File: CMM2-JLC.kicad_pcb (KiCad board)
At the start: 2 copper layers, 49 parts, among them J1 Nunchuck, U1 STM32H743IITx, U2 MT48LC16M16A2P

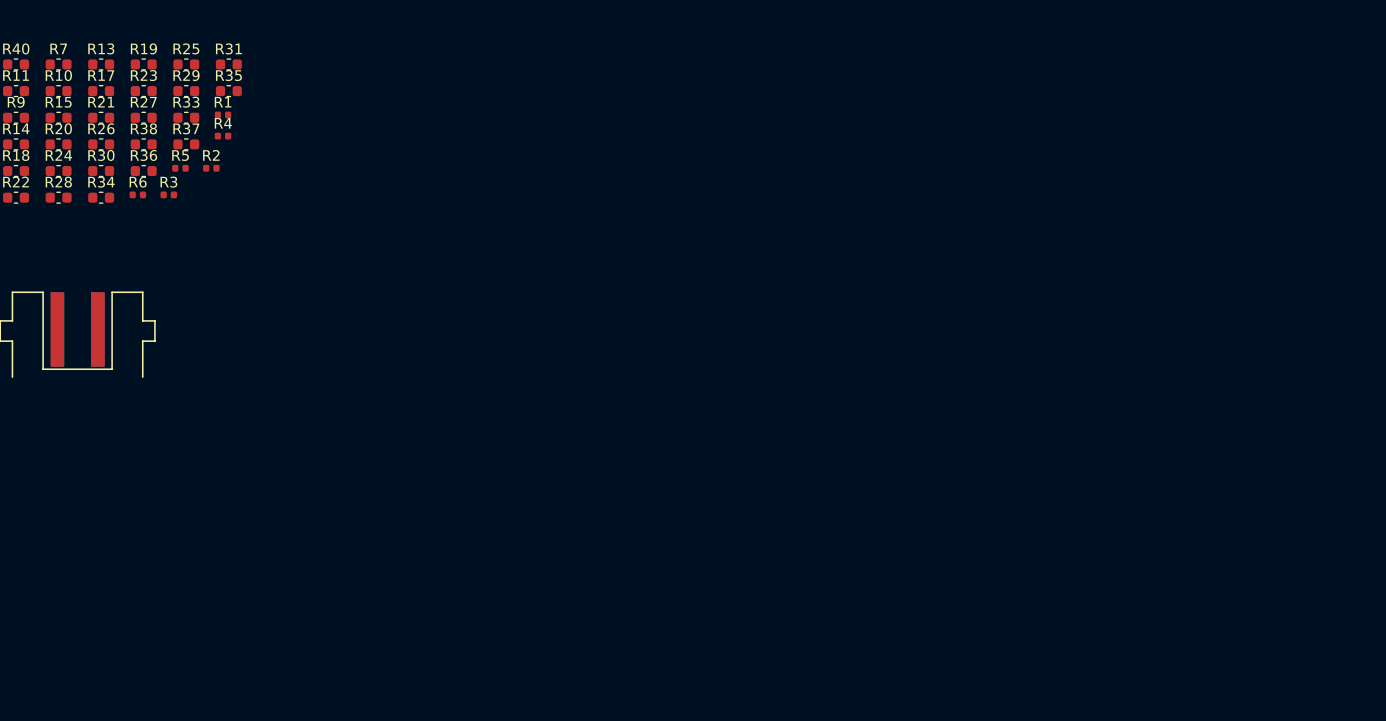
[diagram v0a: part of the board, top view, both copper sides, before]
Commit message: Add footprints and crystals
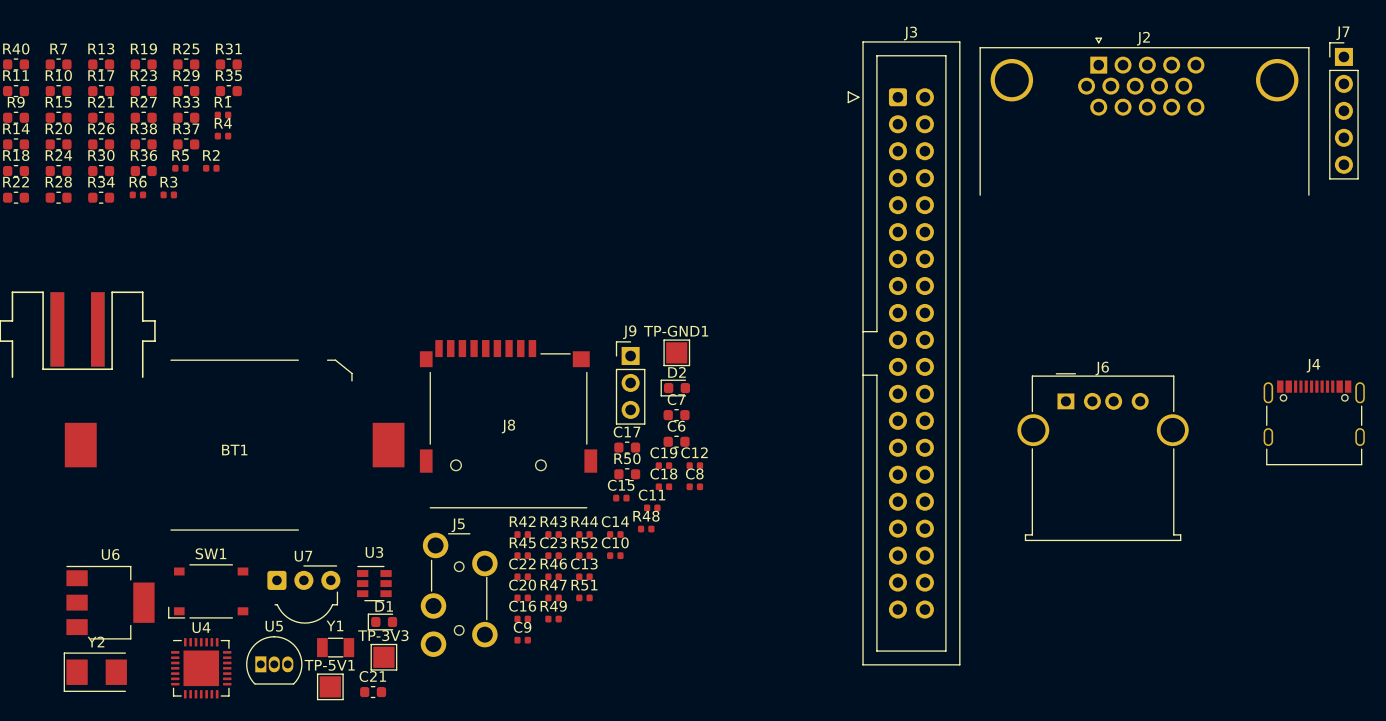
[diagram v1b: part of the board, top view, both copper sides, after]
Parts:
- added BT1: CR2032, CMM2-JLC:BatteryHolder_CR2032-BS-6-1, F.Cu at (110.4, 65.5)
- added C10: 6p, Capacitor_SMD:C_0402_1005Metric, F.Cu at (146.3, 75.9)
- added C11: 20p, Capacitor_SMD:C_0402_1005Metric, F.Cu at (149.7, 71.4)
- added C12: 20p, Capacitor_SMD:C_0402_1005Metric, F.Cu at (153.8, 67.4)
- added C13: 1u, Capacitor_SMD:C_0402_1005Metric, F.Cu at (143.3, 77.9)
- added C14: 100n, Capacitor_SMD:C_0402_1005Metric, F.Cu at (146.3, 73.9)
- added C15: 4.7u, Capacitor_SMD:C_0402_1005Metric, F.Cu at (146.8, 70.5)
- added C16: 100n, Capacitor_SMD:C_0402_1005Metric, F.Cu at (137.5, 81.9)
- added C17: 10u, Capacitor_SMD:C_0603_1608Metric, F.Cu at (147.4, 65.7)
- added C18: 100n, Capacitor_SMD:C_0402_1005Metric, F.Cu at (150.8, 69.4)
- added C19: 1u, Capacitor_SMD:C_0402_1005Metric, F.Cu at (150.8, 67.4)
- added C20: 100n, Capacitor_SMD:C_0402_1005Metric, F.Cu at (137.5, 79.9)
- added C21: 22u, Capacitor_SMD:C_0603_1608Metric, F.Cu at (123.4, 88.8)
- added C22: 100n, Capacitor_SMD:C_0402_1005Metric, F.Cu at (137.5, 77.9)
- added C23: 100n, Capacitor_SMD:C_0402_1005Metric, F.Cu at (140.4, 75.9)
- added C6: 2.2u, Capacitor_SMD:C_0603_1608Metric, F.Cu at (152.0, 65.2)
- added C7: 2.2u, Capacitor_SMD:C_0603_1608Metric, F.Cu at (152.0, 62.7)
- added C8: 1u, Capacitor_SMD:C_0402_1005Metric, F.Cu at (153.8, 69.4)
- added C9: 6p, Capacitor_SMD:C_0402_1005Metric, F.Cu at (137.5, 83.9)
- added D1: SD CARD / RED, LED_SMD:LED_0603_1608Metric, F.Cu at (124.5, 82.2)
- added D2: POWER / GREEN, LED_SMD:LED_0603_1608Metric, F.Cu at (152.1, 60.1)
- added J2: VGA, Connector_Dsub:DSUB-15-HD_Male_Horizontal_P2.29x1.98mm_EdgePinOffset8.35mm_Housed_MountingHolesOffset10.89mm, F.Cu at (191.8, 29.7)
- added J3: EXTERNAL I/O, Connector_IDC:IDC-Header_2x20_P2.54mm_Vertical, F.Cu at (172.9, 32.7)
- added J4: USB_C_Receptacle_USB2.0, Connector_USB:USB_C_Receptacle_Palconn_UTC16-G, F.Cu at (212.1, 62.5)
- added J5: Audio, CMM2-JLC:PJ-3270, F.Cu at (131.6, 86.0)
- added J6: USB A Host, Connector_USB:USB_A_Molex_67643_Horizontal, F.Cu at (188.7, 61.4)
- added J7: SWD, Connector_PinHeader_2.54mm:PinHeader_1x05_P2.54mm_Vertical, F.Cu at (214.9, 28.9)
- added J8: Micro_SD_Card_Det, CMM2-JLC:HOAUC_HYC77-TF09-200, F.Cu at (131.2, 67.4)
- added J9: Boot select, Connector_PinHeader_2.54mm:PinHeader_1x03_P2.54mm_Vertical, F.Cu at (147.7, 57.1)
- added R42: 10k, Resistor_SMD:R_0402_1005Metric, F.Cu at (137.5, 73.9)
- added R43: 10R, Resistor_SMD:R_0402_1005Metric, F.Cu at (140.4, 73.9)
- added R44: 5.1k, Resistor_SMD:R_0402_1005Metric, F.Cu at (143.3, 73.9)
- added R45: 5.1k, Resistor_SMD:R_0402_1005Metric, F.Cu at (137.5, 75.9)
- added R46: 4.7k, Resistor_SMD:R_0402_1005Metric, F.Cu at (140.4, 77.9)
- added R47: 3.3k, Resistor_SMD:R_0402_1005Metric, F.Cu at (140.4, 79.9)
- added R48: 4.7k, Resistor_SMD:R_0402_1005Metric, F.Cu at (149.2, 73.4)
- added R49: 4.7k, Resistor_SMD:R_0402_1005Metric, F.Cu at (140.4, 81.9)
- added R50: 120R, Resistor_SMD:R_0603_1608Metric, F.Cu at (147.4, 68.2)
- added R51: 100k, Resistor_SMD:R_0402_1005Metric, F.Cu at (143.3, 79.9)
- added R52: 10k, Resistor_SMD:R_0402_1005Metric, F.Cu at (143.3, 75.9)
- added SW1: Reset, CMM2-JLC:TS-1187A-X-X-X, F.Cu at (108.2, 79.3)
- added TP-3V3: TestPoint, TestPoint:TestPoint_Pad_2.0x2.0mm, F.Cu at (124.5, 85.5)
- added TP-5V1: TestPoint, TestPoint:TestPoint_Pad_2.0x2.0mm, F.Cu at (119.4, 88.3)
- added TP-GND1: TestPoint, TestPoint:TestPoint_Pad_2.0x2.0mm, F.Cu at (152.1, 56.8)
- added U3: SRV05-4, Package_TO_SOT_SMD:SOT-23-6, F.Cu at (123.6, 78.5)
- added U4: CP2102N-A01-GQFN28, Package_DFN_QFN:QFN-28-1EP_5x5mm_P0.5mm_EP3.35x3.35mm, F.Cu at (107.2, 86.5)
- added U5: DS18B20, Package_TO_SOT_THT:TO-92_Inline, F.Cu at (112.9, 86.2)
- added U6: AMS1117-3.3, Package_TO_SOT_SMD:SOT-223-3_TabPin2, F.Cu at (98.7, 80.3)
- added U7: TSOP4838, OptoDevice:Vishay_MOLD-3Pin, F.Cu at (114.4, 78.2)
- added Y1: 32.768 kHz, Crystal:Crystal_SMD_3215-2Pin_3.2x1.5mm, F.Cu at (119.9, 84.6)
- added Y2: 8 MHz, Crystal:Crystal_SMD_5032-2Pin_5.0x3.2mm, F.Cu at (97.4, 86.9)
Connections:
- net Net-(U1-Pad119) renamed /PA8
- U1 pad 120: Net-(U1-Pad120) -> /PA9
- U1 pad 121: Net-(U1-Pad121) -> /PA10
- U1 pad 122: Net-(U1-Pad122) -> /PA11
- U1 pad 123: Net-(U1-Pad123) -> /PA12
- U1 pad 124: Net-(U1-Pad124) -> /PA13
- U1 pad 137: Net-(U1-Pad137) -> /PA14
- U1 pad 138: Net-(U1-Pad138) -> /PA15
- U1 pad 166: Net-(U1-Pad166) -> /BOOT0
- U1 pad 31: Net-(U1-Pad31) -> /RESET
- U1 pad 40: Net-(U1-Pad40) -> /PA0
- U1 pad 41: Net-(U1-Pad41) -> /PA1
- U1 pad 42: Net-(U1-Pad42) -> /PA2
- U1 pad 47: Net-(U1-Pad47) -> /PA3
- U1 pad 50: Net-(U1-Pad50) -> /PA4
- U1 pad 51: Net-(U1-Pad51) -> /PA5
- U1 pad 52: Net-(U1-Pad52) -> /PA6
- U1 pad 53: Net-(U1-Pad53) -> /PA7
- U1 pad 6: Net-(U1-Pad6) -> /VBAT
- U1 pad 89: /PH12 -> GND

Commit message: Add board outline
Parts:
- moved J7 297.8 mm to (512.7, 30.5)
- moved R48 297.8 mm to (447.0, 75.0)
- moved C1 297.8 mm to (329.8, 59.2)
- moved C10 297.8 mm to (444.1, 77.5)
- moved C11 297.8 mm to (447.5, 73.0)
- moved C12 297.8 mm to (451.6, 69.0)
- moved C14 297.8 mm to (444.1, 75.5)
- moved C17 297.8 mm to (445.2, 67.3)
- moved C21 297.8 mm to (421.2, 90.4)
- moved C23 297.8 mm to (438.2, 77.5)
- moved C4 297.8 mm to (329.8, 61.2)
- moved C8 297.8 mm to (451.6, 71.0)
- moved D2 297.8 mm to (449.9, 61.7)
- moved J2 297.8 mm to (489.6, 31.3)
- moved J3 297.8 mm to (470.7, 34.3)
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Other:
- board outline added: 130 x 102 mm
- copper layers 2 -> 4
- net class Default: clearance 0.2 -> 0.127; trace_width 0.25 -> 0.127; via_dia 0.8 -> 0.45; via_drill 0.4 -> 0.2
- rule pad_to_mask_clearance: 0.05 -> 0.01
- rule trace_clearance: 0.2 -> 0.127
- rule trace_min: 0.2 -> 0.127
- rule via_min_drill: 0.3 -> 0.2
- rule via_min_size: 0.4 -> 0.45

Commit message: first sdram routing
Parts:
- removed BT1: CR2032, CMM2-JLC:BatteryHolder_CR2032-BS-6-1
- removed C1, C14, C16, C18, C2, C20, C22, C23, C3, C4, C5: 100n, Capacitor_SMD:C_0402_1005Metric
- removed C10, C9: 6p, Capacitor_SMD:C_0402_1005Metric
- removed C11, C12: 20p, Capacitor_SMD:C_0402_1005Metric
- removed C13, C19, C8: 1u, Capacitor_SMD:C_0402_1005Metric
- removed C15: 4.7u, Capacitor_SMD:C_0402_1005Metric
- removed C17: 10u, Capacitor_SMD:C_0603_1608Metric
- removed C21: 22u, Capacitor_SMD:C_0603_1608Metric
- removed C6, C7: 2.2u, Capacitor_SMD:C_0603_1608Metric
- removed D1: SD CARD / RED, LED_SMD:LED_0603_1608Metric
- removed D2: POWER / GREEN, LED_SMD:LED_0603_1608Metric
- removed J2: VGA, Connector_Dsub:DSUB-15-HD_Male_Horizontal_P2.29x1.98mm_EdgePinOffset8.35mm_Housed_MountingHolesOffset10.89mm
- removed J3: EXTERNAL I/O, Connector_IDC:IDC-Header_2x20_P2.54mm_Vertical
- removed J4: USB_C_Receptacle_USB2.0, Connector_USB:USB_C_Receptacle_Palconn_UTC16-G
- removed J5: Audio, CMM2-JLC:PJ-3270
- removed J6: USB A Host, Connector_USB:USB_A_Molex_67643_Horizontal
- removed J7: SWD, Connector_PinHeader_2.54mm:PinHeader_1x05_P2.54mm_Vertical
- removed J8: Micro_SD_Card_Det, CMM2-JLC:HOAUC_HYC77-TF09-200
- removed J9: Boot select, Connector_PinHeader_2.54mm:PinHeader_1x03_P2.54mm_Vertical
- removed R1, R2, R3, R4, R42, R5, R52, R6: 10k, Resistor_SMD:R_0402_1005Metric
- removed R10, R11, R12, R16, R17, R18, R22, R23, R24, R28, R29, R30, R34, R36, R37, R40, R7, R8, R9: 240R, Resistor_SMD:R_0603_1608Metric
- removed R13, R14, R15, R19, R20, R21, R25, R26, R27, R31, R32, R33, R39, R50: 120R, Resistor_SMD:R_0603_1608Metric
- removed R35, R38, R41: 75R, Resistor_SMD:R_0603_1608Metric
- removed R43: 10R, Resistor_SMD:R_0402_1005Metric
- removed R44, R45: 5.1k, Resistor_SMD:R_0402_1005Metric
- removed R46, R48, R49: 4.7k, Resistor_SMD:R_0402_1005Metric
- removed R47: 3.3k, Resistor_SMD:R_0402_1005Metric
- removed R51: 100k, Resistor_SMD:R_0402_1005Metric
- removed SW1: Reset, CMM2-JLC:TS-1187A-X-X-X
- removed TP-3V3, TP-5V1, TP-GND1: TestPoint, TestPoint:TestPoint_Pad_2.0x2.0mm
- removed U3: SRV05-4, Package_TO_SOT_SMD:SOT-23-6
- removed U4: CP2102N-A01-GQFN28, Package_DFN_QFN:QFN-28-1EP_5x5mm_P0.5mm_EP3.35x3.35mm
- removed U5: DS18B20, Package_TO_SOT_THT:TO-92_Inline
- removed U6: AMS1117-3.3, Package_TO_SOT_SMD:SOT-223-3_TabPin2
- removed U7: TSOP4838, OptoDevice:Vishay_MOLD-3Pin
- removed Y1: 32.768 kHz, Crystal:Crystal_SMD_3215-2Pin_3.2x1.5mm
- removed Y2: 8 MHz, Crystal:Crystal_SMD_5032-2Pin_5.0x3.2mm
- moved U2 271.3 mm to (86.0, 92.0)
- moved U1 257.6 mm to (86.0, 67.1)
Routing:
- net /PF5: track 0.00 -> 34.7 mm, vias 0 -> 2
- net /PG1: track 0.00 -> 34.6 mm
- net /PF15: track 0.00 -> 34.4 mm
- net /PF4: track 0.00 -> 34.4 mm, vias 0 -> 2
- net /PF14: track 0.00 -> 33.9 mm
- net /PF13: track 0.00 -> 32.8 mm
- net /PF0: track 0.00 -> 29.4 mm, vias 0 -> 2
- net /PF1: track 0.00 -> 28.5 mm, vias 0 -> 2
- net /PF2: track 0.00 -> 27.3 mm, vias 0 -> 2
- net /PF3: track 0.00 -> 26.2 mm, vias 0 -> 2
- net /PF12: track 0.00 -> 5.13 mm
- net /PG0: track 0.00 -> 1.25 mm, vias 0 -> 1
- added copper zone on POWER, net +3V3
- added copper zone on GND, net GND

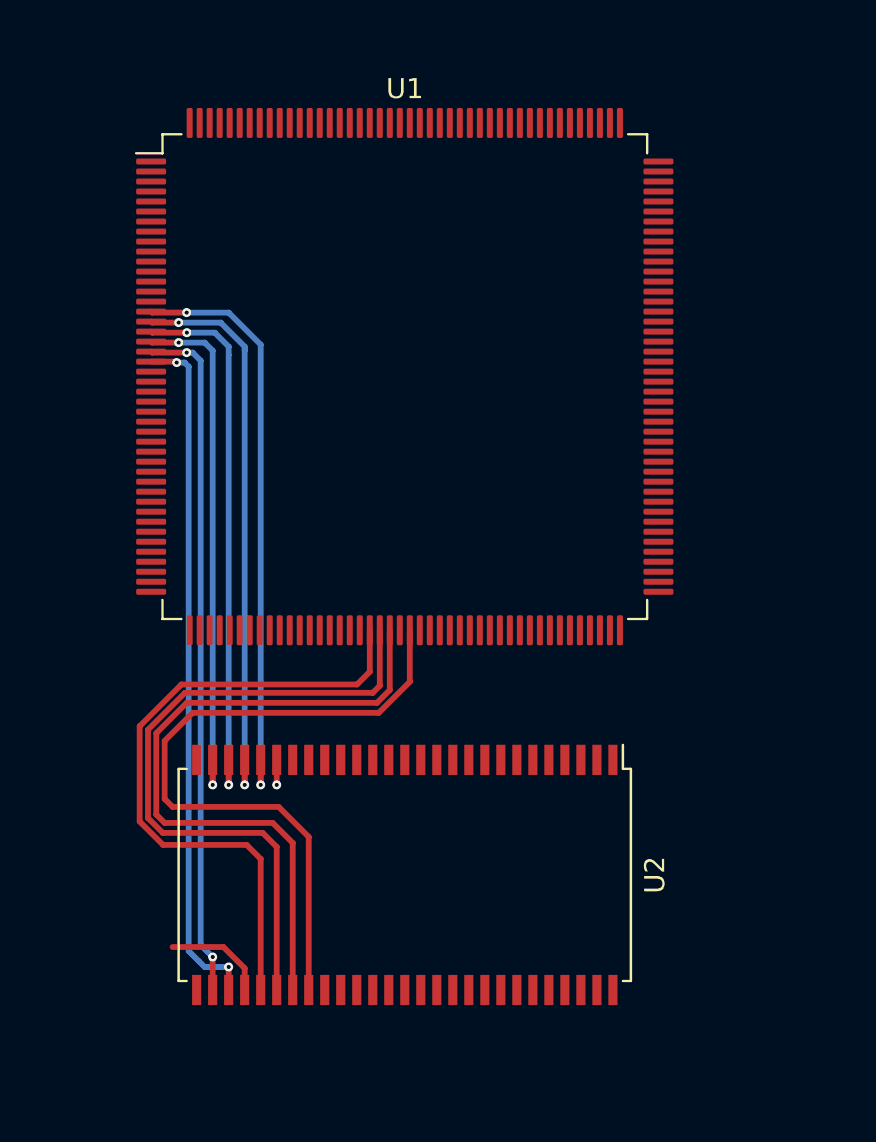
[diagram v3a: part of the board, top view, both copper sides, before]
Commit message: sdram routed
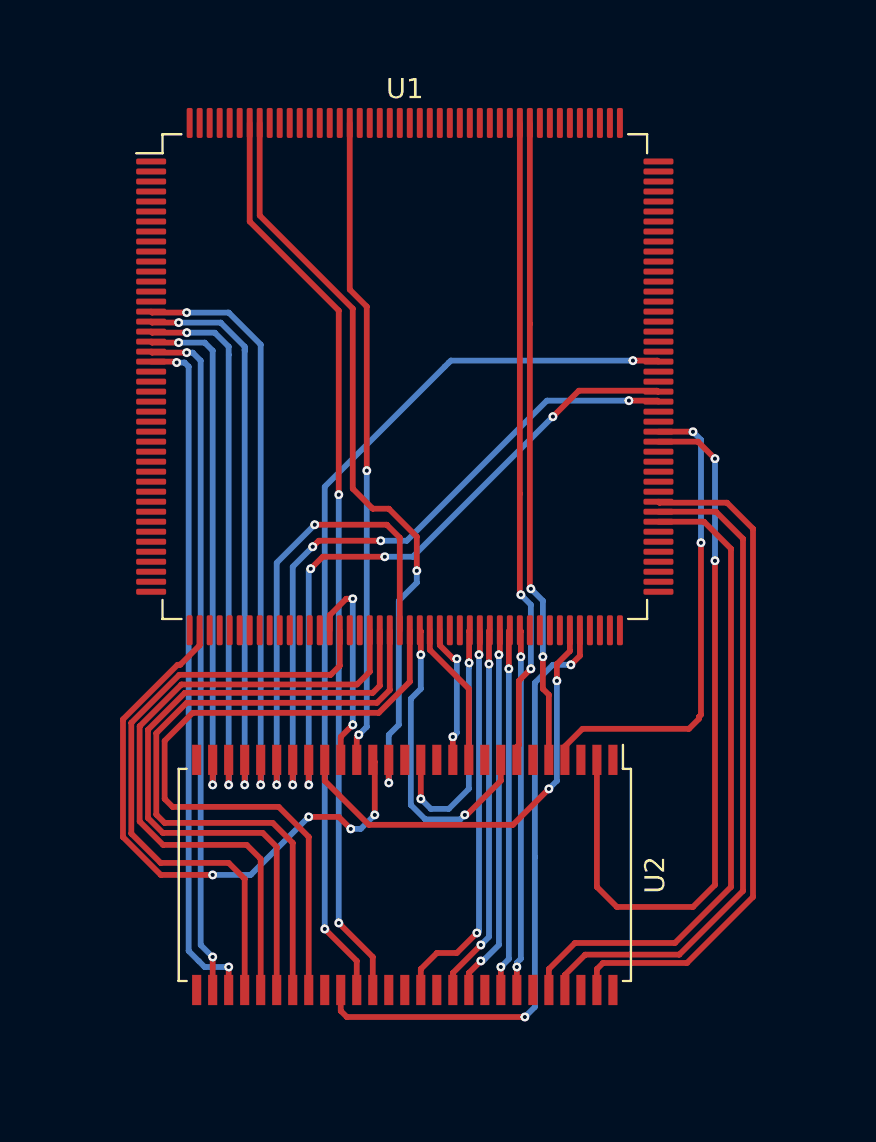
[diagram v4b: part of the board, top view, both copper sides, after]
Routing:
- net /PE1: track 0.00 -> 45.9 mm, vias 0 -> 2
- net /PG8: track 0.00 -> 45.1 mm, vias 0 -> 2
- net /PE0: track 0.00 -> 38.4 mm, vias 0 -> 2
- net /PD14: track 0.00 -> 37.6 mm, vias 0 -> 2
- net /PD10: track 0.00 -> 34.0 mm
- net /PG4: track 0.00 -> 33.9 mm, vias 0 -> 4
- net /PD9: track 0.00 -> 33.8 mm
- net /PG5: track 0.00 -> 33.2 mm, vias 0 -> 4
- net /PD8: track 0.00 -> 32.9 mm
- net /PG15: track 0.00 -> 32.4 mm, vias 0 -> 2
- net /PD1: track 0.00 -> 32.3 mm, vias 0 -> 2
- net /PD0: track 0.00 -> 32.2 mm, vias 0 -> 2
- net /PH7: track 0.00 -> 31.4 mm, vias 0 -> 2
- net /PH5: track 0.00 -> 29.9 mm, vias 0 -> 4
- net /PF12: track 5.13 -> 31.1 mm
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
